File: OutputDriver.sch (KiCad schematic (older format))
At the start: 8 parts, among them IC2 DRV135UA_2K5, J3 XLR3_Ground

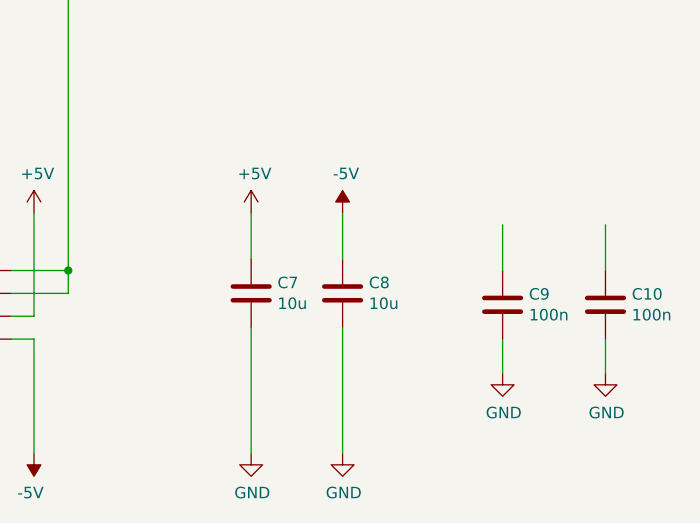
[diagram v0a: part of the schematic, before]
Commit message: selecting actual components
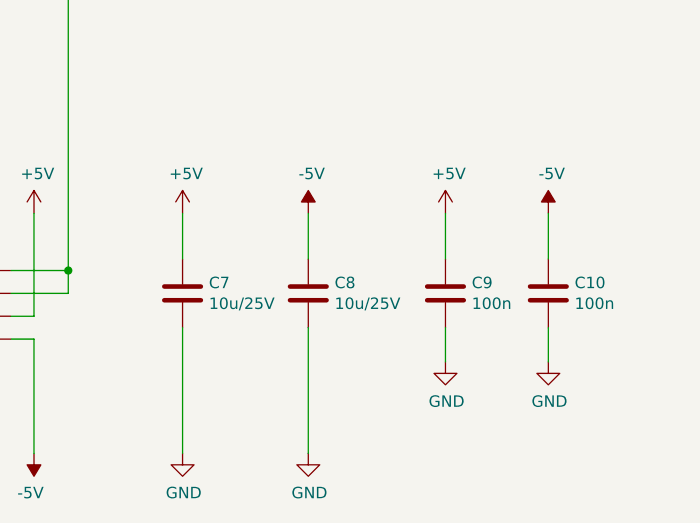
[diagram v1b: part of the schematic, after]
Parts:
- C7, C8: value 10u -> 10u/25V; footprint (none) -> Resistor_SMD:R_0805_2012Metric; PN (none) -> TMK212BBJ106MG-T
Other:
- moved on the sheet: C10, C7, C8, C9
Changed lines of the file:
@@
 EESchema Schematic File Version 4
+LIBS:BalancedAudioBox-cache
 EELAYER 29 0
 EELAYER END
@@
 L power:+5V #PWR021
 U 1 1 5D3E5853
-P 5100 2700
-F 0 "#PWR021" H 5100 2550 50  0001 C CNN
-F 1 "+5V" H 5115 2873 50  0000 C CNN
-F 2 "" H 5100 2700 50  0001 C CNN
-F 3 "" H 5100 2700 50  0001 C CNN
-	1    5100 2700
+P 4800 2700
+F 0 "#PWR021" H 4800 2550 50  0001 C CNN
+F 1 "+5V" H 4815 2873 50  0000 C CNN
+F 2 "" H 4800 2700 50  0001 C CNN
+F 3 "" H 4800 2700 50  0001 C CNN
+	1    4800 2700
 	1    0    0    -1
 $EndComp
@@
 L power:-5V #PWR023
 U 1 1 5D3E5E79
-P 5500 2700
-F 0 "#PWR023" H 5500 2800 50  0001 C CNN
-F 1 "-5V" H 5515 2873 50  0000 C CNN
-F 2 "" H 5500 2700 50  0001 C CNN
-F 3 "" H 5500 2700 50  0001 C CNN
-	1    5500 2700
+P 5350 2700
+F 0 "#PWR023" H 5350 2800 50  0001 C CNN
+F 1 "-5V" H 5365 2873 50  0000 C CNN
+F 2 "" H 5350 2700 50  0001 C CNN
+F 3 "" H 5350 2700 50  0001 C CNN
+	1    5350 2700
 	1    0    0    -1
 $EndComp
@@
 L Device:C C7
 U 1 1 5D3E6452
-P 5100 3050
-F 0 "C7" H 5215 3096 50  0000 L CNN
-F 1 "10u" H 5215 3005 50  0000 L CNN
-F 2 "" H 5138 2900 50  0001 C CNN
-F 3 "~" H 5100 3050 50  0001 C CNN
-	1    5100 3050
+P 4800 3050
+F 0 "C7" H 4915 3096 50  0000 L CNN
+F 1 "10u/25V" H 4915 3005 50  0000 L CNN
+F 2 "Resistor_SMD:R_0805_2012Metric" H 4838 2900 50  0001 C CNN
+F 3 "~" H 4800 3050 50  0001 C CNN
+F 4 "TMK212BBJ106MG-T" H 4800 3050 50  0001 C CNN "PN"
+	1    4800 3050
 	1    0    0    -1
 $EndComp
@@
 L Device:C C8
 U 1 1 5D3E6A96
-P 5500 3050
-F 0 "C8" H 5615 3096 50  0000 L CNN
-F 1 "10u" H 5615 3005 50  0000 L CNN
-F 2 "" H 5538 2900 50  0001 C CNN
-F 3 "~" H 5500 3050 50  0001 C CNN
-	1    5500 3050
+P 5350 3050
+F 0 "C8" H 5465 3096 50  0000 L CNN
+F 1 "10u/25V" H 5465 3005 50  0000 L CNN
+F 2 "Resistor_SMD:R_0805_2012Metric" H 5388 2900 50  0001 C CNN
+F 3 "~" H 5350 3050 50  0001 C CNN
+F 4 "TMK212BBJ106MG-T" H 5350 3050 50  0001 C CNN "PN"
+	1    5350 3050
 	1    0    0    -1
 $EndComp
@@
 L power:GND #PWR022
 U 1 1 5D3E6F05
-P 5100 3750
-F 0 "#PWR022" H 5100 3500 50  0001 C CNN
-F 1 "GND" H 5105 3577 50  0000 C CNN
-F 2 "" H 5100 3750 50  0001 C CNN
-F 3 "" H 5100 3750 50  0001 C CNN
-	1    5100 3750
+P 4800 3750
+F 0 "#PWR022" H 4800 3500 50  0001 C CNN
+F 1 "GND" H 4805 3577 50  0000 C CNN
+F 2 "" H 4800 3750 50  0001 C CNN
+F 3 "" H 4800 3750 50  0001 C CNN
+	1    4800 3750
 	1    0    0    -1
 $EndComp
@@
 L power:GND #PWR024
 U 1 1 5D3E73E6
-P 5500 3750
-F 0 "#PWR024" H 5500 3500 50  0001 C CNN
-F 1 "GND" H 5505 3577 50  0000 C CNN
-F 2 "" H 5500 3750 50  0001 C CNN
-F 3 "" H 5500 3750 50  0001 C CNN
-	1    5500 3750
-	1    0    0    -1
-$EndComp
-Wire Wire Line
-	5500 3750 5500 3200
-Wire Wire Line
-	5500 2900 5500 2700
-Wire Wire Line
-	5100 2700 5100 2900
-Wire Wire Line
-	5100 3200 5100 3750
+P 5350 3750
+F 0 "#PWR024" H 5350 3500 50  0001 C CNN
+F 1 "GND" H 5355 3577 50  0000 C CNN
+F 2 "" H 5350 3750 50  0001 C CNN
+F 3 "" H 5350 3750 50  0001 C CNN
+	1    5350 3750
+	1    0    0    -1
+$EndComp
+Wire Wire Line
+	5350 3750 5350 3200
+Wire Wire Line
+	5350 2900 5350 2700
+Wire Wire Line
+	4800 2700 4800 2900
+Wire Wire Line
+	4800 3200 4800 3750
 $Comp
 L power:GND #PWR017
@@
 L Device:C C?
 U 1 1 5D43B3A7
-P 6200 3100
+P 5950 3050
 AR Path="/5D41DA57/5D43B3A7" Ref="C?"  Part="1"
 AR Path="/5D3D9E6F/5D43B3A7" Ref="C9"  Part="1"
-F 0 "C9" H 6315 3146 50  0000 L CNN
-F 1 "100n" H 6315 3055 50  0000 L CNN
-F 2 "Capacitor_SMD:C_0603_1608Metric" H 6238 2950 50  0001 C CNN
-F 3 "~" H 6200 3100 50  0001 C CNN
-	1    6200 3100
+F 0 "C9" H 6065 3096 50  0000 L CNN
+F 1 "100n" H 6065 3005 50  0000 L CNN
+F 2 "Capacitor_SMD:C_0603_1608Metric" H 5988 2900 50  0001 C CNN
+F 3 "~" H 5950 3050 50  0001 C CNN
+	1    5950 3050
 	1    0    0    -1
 $EndComp
@@
 L Device:C C?
 U 1 1 5D43B3AD
-P 6650 3100
+P 6400 3050
 AR Path="/5D41DA57/5D43B3AD" Ref="C?"  Part="1"
 AR Path="/5D3D9E6F/5D43B3AD" Ref="C10"  Part="1"
-F 0 "C10" H 6765 3146 50  0000 L CNN
-F 1 "100n" H 6765 3055 50  0000 L CNN
-F 2 "Capacitor_SMD:C_0603_1608Metric" H 6688 2950 50  0001 C CNN
-F 3 "~" H 6650 3100 50  0001 C CNN
-	1    6650 3100
+F 0 "C10" H 6515 3096 50  0000 L CNN
+F 1 "100n" H 6515 3005 50  0000 L CNN
+F 2 "Capacitor_SMD:C_0603_1608Metric" H 6438 2900 50  0001 C CNN
+F 3 "~" H 6400 3050 50  0001 C CNN
+	1    6400 3050
 	1    0    0    -1
 $EndComp
@@
 L power:GND #PWR?
 U 1 1 5D43B3BF
-P 6200 3400
+P 5950 3350
 AR Path="/5D41DA57/5D43B3BF" Ref="#PWR?"  Part="1"
 AR Path="/5D3D9E6F/5D43B3BF" Ref="#PWR025"  Part="1"
-F 0 "#PWR025" H 6200 3150 50  0001 C CNN
-F 1 "GND" H 6205 3227 50  0000 C CNN
-F 2 "" H 6200 3400 50  0001 C CNN
-F 3 "" H 6200 3400 50  0001 C CNN
-	1    6200 3400
+F 0 "#PWR025" H 5950 3100 50  0001 C CNN
+F 1 "GND" H 5955 3177 50  0000 C CNN
+F 2 "" H 5950 3350 50  0001 C CNN
+F 3 "" H 5950 3350 50  0001 C CNN
+	1    5950 3350
 	1    0    0    -1
 $EndComp
@@
 L power:GND #PWR?
 U 1 1 5D43B3C5
-P 6650 3400
+P 6400 3350
 AR Path="/5D41DA57/5D43B3C5" Ref="#PWR?"  Part="1"
 AR Path="/5D3D9E6F/5D43B3C5" Ref="#PWR026"  Part="1"
-F 0 "#PWR026" H 6650 3150 50  0001 C CNN
-F 1 "GND" H 6655 3227 50  0000 C CNN
-F 2 "" H 6650 3400 50  0001 C CNN
-F 3 "" H 6650 3400 50  0001 C CNN
-	1    6650 3400
-	1    0    0    -1
-$EndComp
-Wire Wire Line
-	6200 3400 6200 3250
-Wire Wire Line
-	6650 3400 6650 3250
-Wire Wire Line
-	6650 2950 6650 2750
-Wire Wire Line
-	6200 2950 6200 2750
+F 0 "#PWR026" H 6400 3100 50  0001 C CNN
+F 1 "GND" H 6405 3177 50  0000 C CNN
+F 2 "" H 6400 3350 50  0001 C CNN
+F 3 "" H 6400 3350 50  0001 C CNN
+	1    6400 3350
+	1    0    0    -1
+$EndComp
+Wire Wire Line
+	5950 3350 5950 3200
+Wire Wire Line
+	6400 3350 6400 3200
+Wire Wire Line
+	6400 2900 6400 2700
+Wire Wire Line
+	5950 2900 5950 2700
 Text Notes 5150 1200 0    50   ~ 0
 minimum supply for +4dBu = 4.5V
+$Comp
+L power:+5V #PWR?
+U 1 1 5D44429E
+P 5950 2700
+F 0 "#PWR?" H 5950 2550 50  0001 C CNN
+F 1 "+5V" H 5965 2873 50  0000 C CNN
+F 2 "" H 5950 2700 50  0001 C CNN
+F 3 "" H 5950 2700 50  0001 C CNN
+	1    5950 2700
+	1    0    0    -1
+$EndComp
+$Comp
+L power:-5V #PWR?
+U 1 1 5D4446B5
+P 6400 2700
+F 0 "#PWR?" H 6400 2800 50  0001 C CNN
+F 1 "-5V" H 6415 2873 50  0000 C CNN
+F 2 "" H 6400 2700 50  0001 C CNN
+F 3 "" H 6400 2700 50  0001 C CNN
+	1    6400 2700
+	1    0    0    -1
+$EndComp
 $EndSCHEMATC

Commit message: work
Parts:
- added C23, C24: 4.7u, Capacitor_SMD:C_0805_2012Metric, symbol Device:C
- added C25, C26: 100n, Capacitor_SMD:C_0603_1608Metric, symbol Device:C
- added IC3: DRV135UA_2K5, SamacSys_PCB_Library:SOIC127P600X175-8N, symbol BalancedAudioBox:DRV135UA_2K5
- added J4: XLR3_Ground, symbol Connector:XLR3_Ground
- added R16, R17: 300R, Resistor_SMD:R_0603_1608Metric, symbol Device:R
- C7, C8: value 10u/25V -> 4.7u; footprint Resistor_SMD:R_0805_2012Metric -> Capacitor_SMD:C_0805_2012Metric; PN TMK212BBJ106MG-T -> (none)
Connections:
- net +5V: now also C23.1, C25.1, IC3.6 (V+)
- net -5V: now also C24.1, C26.1, IC3.5 (V-)
- net GND: now also C23.2, C24.2, C25.2, C26.2, IC3.3 (GND), J4.1, J4.G
- new net: IC3.1 (-V0), IC3.2 (-SENSE), R16.1
- new net: IC3.7 (+SENSE), IC3.8 (+V0), R17.2
- new net: J4.2, R17.1
- new net: J4.3, R16.2
- new net RIGHT: IC3.4 (VIN)

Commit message: adding PCB libraries
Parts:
- J3, J4: footprint (none) -> BalancedAudioBox:XLR-NC3MA
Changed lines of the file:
@@
 F 0 "J3" H 3150 2015 50  0000 C CNN
 F 1 "XLR3_Ground" H 3150 1924 50  0000 C CNN
-F 2 "" H 3150 1650 50  0001 C CNN
+F 2 "BalancedAudioBox:XLR-NC3MA" H 3150 1650 50  0001 C CNN
 F 3 " ~" H 3150 1650 50  0001 C CNN
 	1    3150 1650
@@
 F 0 "J4" H 3150 4965 50  0000 C CNN
 F 1 "XLR3_Ground" H 3150 4874 50  0000 C CNN
-F 2 "" H 3150 4600 50  0001 C CNN
+F 2 "BalancedAudioBox:XLR-NC3MA" H 3150 4600 50  0001 C CNN
 F 3 " ~" H 3150 4600 50  0001 C CNN
 	1    3150 4600

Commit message: placement complete
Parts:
- C10, C25, C26, C9: footprint Capacitor_SMD:C_0603_1608Metric -> Capacitor_SMD:C_0402_1005Metric
- IC2, IC3: footprint SamacSys_PCB_Library:SOIC127P600X175-8N -> Package_SO:SOIC-8_3.9x4.9mm_P1.27mm
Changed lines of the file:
@@
 F 0 "IC2" H 3400 3215 50  0000 C CNN
 F 1 "DRV135UA_2K5" H 3400 3124 50  0000 C CNN
-F 2 "SamacSys_PCB_Library:SOIC127P600X175-8N" H 3900 3050 50  0001 L CNN
+F 2 "Package_SO:SOIC-8_3.9x4.9mm_P1.27mm" H 3900 3050 50  0001 L CNN
 F 3 "http://www.ti.com/lit/gpn/drv135" H 3900 2950 50  0001 L CNN
 F 4 "Audio Balanced Line Drivers" H 3900 2850 50  0001 L CNN "Description"
@@
 F 0 "C9" H 6065 3096 50  0000 L CNN
 F 1 "100n" H 6065 3005 50  0000 L CNN
-F 2 "Capacitor_SMD:C_0603_1608Metric" H 5988 2900 50  0001 C CNN
+F 2 "Capacitor_SMD:C_0402_1005Metric" H 5988 2900 50  0001 C CNN
 F 3 "~" H 5950 3050 50  0001 C CNN
 	1    5950 3050
@@
 F 0 "C10" H 6515 3096 50  0000 L CNN
 F 1 "100n" H 6515 3005 50  0000 L CNN
-F 2 "Capacitor_SMD:C_0603_1608Metric" H 6438 2900 50  0001 C CNN
+F 2 "Capacitor_SMD:C_0402_1005Metric" H 6438 2900 50  0001 C CNN
 F 3 "~" H 6400 3050 50  0001 C CNN
 	1    6400 3050
@@
 F 0 "IC3" H 3400 6165 50  0000 C CNN
 F 1 "DRV135UA_2K5" H 3400 6074 50  0000 C CNN
-F 2 "SamacSys_PCB_Library:SOIC127P600X175-8N" H 3900 6000 50  0001 L CNN
+F 2 "Package_SO:SOIC-8_3.9x4.9mm_P1.27mm" H 3900 6000 50  0001 L CNN
 F 3 "http://www.ti.com/lit/gpn/drv135" H 3900 5900 50  0001 L CNN
 F 4 "Audio Balanced Line Drivers" H 3900 5800 50  0001 L CNN "Description"
@@
 F 0 "C25" H 6065 6046 50  0000 L CNN
 F 1 "100n" H 6065 5955 50  0000 L CNN
-F 2 "Capacitor_SMD:C_0603_1608Metric" H 5988 5850 50  0001 C CNN
+F 2 "Capacitor_SMD:C_0402_1005Metric" H 5988 5850 50  0001 C CNN
 F 3 "~" H 5950 6000 50  0001 C CNN
 	1    5950 6000
@@
 F 0 "C26" H 6515 6046 50  0000 L CNN
 F 1 "100n" H 6515 5955 50  0000 L CNN
-F 2 "Capacitor_SMD:C_0603_1608Metric" H 6438 5850 50  0001 C CNN
+F 2 "Capacitor_SMD:C_0402_1005Metric" H 6438 5850 50  0001 C CNN
 F 3 "~" H 6400 6000 50  0001 C CNN
 	1    6400 6000

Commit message: layout and silk
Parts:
- added J8: Conn_01x03, Connector_PinHeader_2.54mm:PinHeader_1x03_P2.54mm_Vertical, symbol Connector_Generic:Conn_01x03
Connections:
- net GND: now also J8.2 (Pin_2)
- net LEFT: now also J8.1 (Pin_1)
- net RIGHT: now also J8.3 (Pin_3)
- net LEFT_VON: now reaches IC2.1 (-V0), IC2.2 (-SENSE), R5.1
- net LEFT_VOP: now reaches IC2.7 (+SENSE), IC2.8 (+V0), R6.2
- net RIGHT_VON: now reaches IC3.1 (-V0), IC3.2 (-SENSE), R16.1
- net RIGHT_VOP: now reaches IC3.7 (+SENSE), IC3.8 (+V0), R17.2
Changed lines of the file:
@@
 LEFT
 Wire Wire Line
-	2050 3250 2750 3250
+	2050 3250 2250 3250
 $Comp
 L Device:C C?
@@
 RIGHT
 Wire Wire Line
-	2050 6200 2750 6200
+	2050 6200 2250 6200
 $Comp
 L Device:C C?
@@
 	1    0    0    -1
 $EndComp
+Text Label 4300 1650 0    50   ~ 0
+LEFT_VOP
+Text Label 3150 2550 0    50   ~ 0
+LEFT_VON
+Text Label 4300 4600 0    50   ~ 0
+RIGHT_VOP
+Text Label 3150 5500 0    50   ~ 0
+RIGHT_VON
+$Comp
+L Connector_Generic:Conn_01x03 J8
+U 1 1 5D474BC9
+P 1950 4300
+F 0 "J8" H 1868 4617 50  0000 C CNN
+F 1 "Conn_01x03" H 1868 4526 50  0000 C CNN
+F 2 "Connector_PinHeader_2.54mm:PinHeader_1x03_P2.54mm_Vertical" H 1950 4300 50  0001 C CNN
+F 3 "~" H 1950 4300 50  0001 C CNN
+	1    1950 4300
+	-1   0    0    -1
+$EndComp
+Wire Wire Line
+	2150 4200 2250 4200
+Wire Wire Line
+	2250 4200 2250 3250
+Connection ~ 2250 3250
+Wire Wire Line
+	2250 3250 2750 3250
+Wire Wire Line
+	2150 4400 2250 4400
+Wire Wire Line
+	2250 4400 2250 6200
+Connection ~ 2250 6200
+Wire Wire Line
+	2250 6200 2750 6200
+$Comp
+L power:GND #PWR0103
+U 1 1 5D47842A
+P 2400 4500
+F 0 "#PWR0103" H 2400 4250 50  0001 C CNN
+F 1 "GND" H 2405 4327 50  0000 C CNN
+F 2 "" H 2400 4500 50  0001 C CNN
+F 3 "" H 2400 4500 50  0001 C CNN
+	1    2400 4500
+	1    0    0    -1
+$EndComp
+Wire Wire Line
+	2150 4300 2400 4300
+Wire Wire Line
+	2400 4300 2400 4500
 $EndSCHEMATC

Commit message: smaller package, drc
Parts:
- C23, C24, C7, C8: footprint Capacitor_SMD:C_0805_2012Metric -> Capacitor_SMD:C_0603_1608Metric
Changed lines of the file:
@@
 F 0 "C7" H 4915 3096 50  0000 L CNN
 F 1 "4.7u" H 4915 3005 50  0000 L CNN
-F 2 "Capacitor_SMD:C_0805_2012Metric" H 4838 2900 50  0001 C CNN
+F 2 "Capacitor_SMD:C_0603_1608Metric" H 4838 2900 50  0001 C CNN
 F 3 "~" H 4800 3050 50  0001 C CNN
 F 4 "" H 4800 3050 50  0001 C CNN "PN"
@@
 F 0 "C8" H 5465 3096 50  0000 L CNN
 F 1 "4.7u" H 5465 3005 50  0000 L CNN
-F 2 "Capacitor_SMD:C_0805_2012Metric" H 5388 2900 50  0001 C CNN
+F 2 "Capacitor_SMD:C_0603_1608Metric" H 5388 2900 50  0001 C CNN
 F 3 "~" H 5350 3050 50  0001 C CNN
 F 4 "" H 5350 3050 50  0001 C CNN "PN"
@@
 F 0 "C23" H 4915 6046 50  0000 L CNN
 F 1 "4.7u" H 4915 5955 50  0000 L CNN
-F 2 "Capacitor_SMD:C_0805_2012Metric" H 4838 5850 50  0001 C CNN
+F 2 "Capacitor_SMD:C_0603_1608Metric" H 4838 5850 50  0001 C CNN
 F 3 "~" H 4800 6000 50  0001 C CNN
 F 4 "" H 4800 6000 50  0001 C CNN "PN"
@@
 F 0 "C24" H 5465 6046 50  0000 L CNN
 F 1 "4.7u" H 5465 5955 50  0000 L CNN
-F 2 "Capacitor_SMD:C_0805_2012Metric" H 5388 5850 50  0001 C CNN
+F 2 "Capacitor_SMD:C_0603_1608Metric" H 5388 5850 50  0001 C CNN
 F 3 "~" H 5350 6000 50  0001 C CNN
 F 4 "" H 5350 6000 50  0001 C CNN "PN"
